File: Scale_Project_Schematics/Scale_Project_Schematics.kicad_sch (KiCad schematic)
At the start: 0 parts

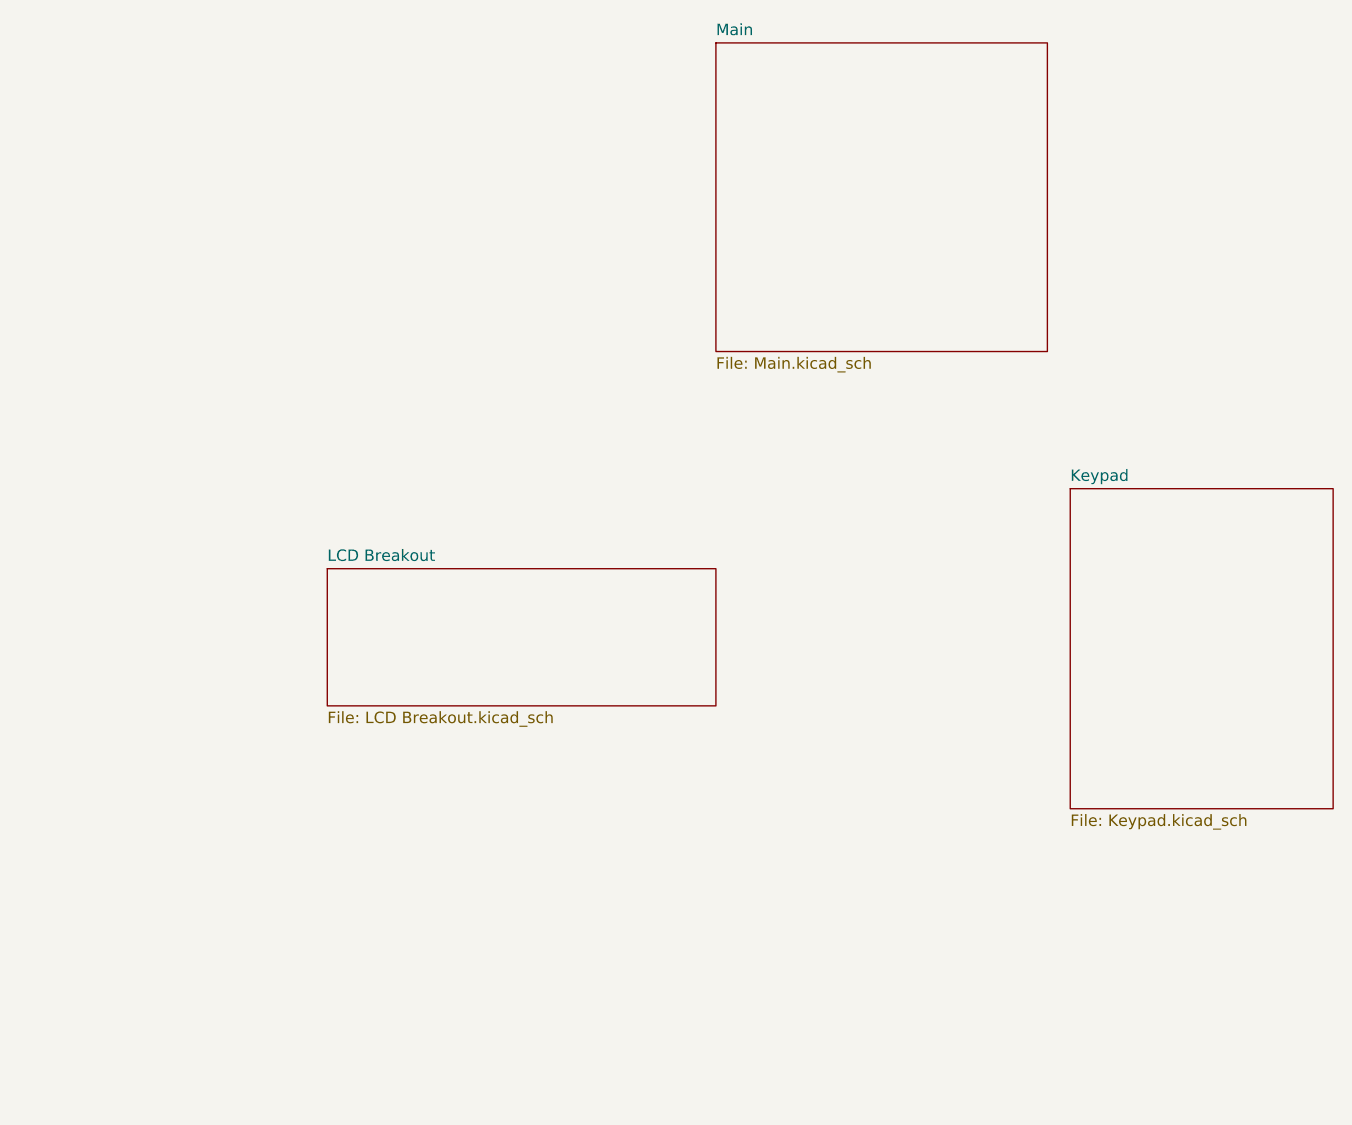
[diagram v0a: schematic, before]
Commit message: Adds Power sheet
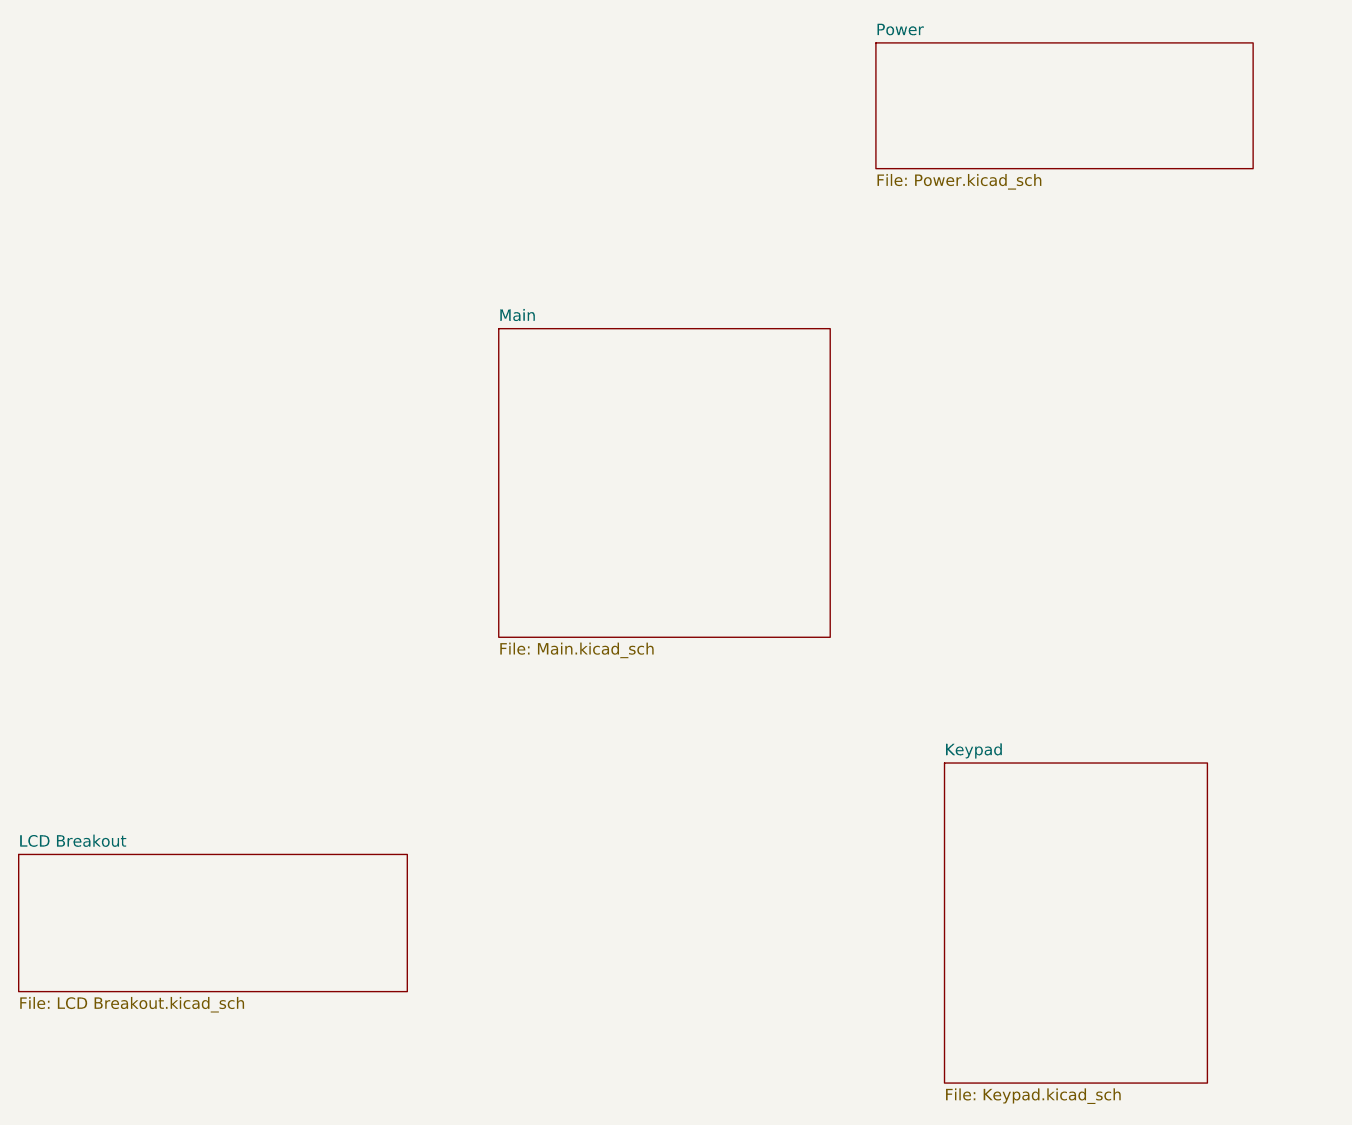
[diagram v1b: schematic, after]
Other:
- added sheet Power (Power.kicad_sch)
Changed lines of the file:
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@@
 	(paper "A4")
 	(sheet
-		(at 160.02 86.36)
+		(at 138.43 36.83)
+		(size 41.91 13.97)
+		(exclude_from_sim no)
+		(in_bom yes)
+		(on_board yes)
+		(dnp no)
+		(fields_autoplaced yes)
+		(stroke
+			(width 0.1524)
+			(type solid)
+		)
+		(fill
+			(color 0 0 0 0.0000)
+		)
+		(property "Sheetname" "Power"
+			(at 138.43 36.1184 0)
+			(effects
+				(font
+					(size 1.27 1.27)
+				)
+				(justify left bottom)
+			)
+		)
+		(property "Sheetfile" "Power.kicad_sch"
+			(at 138.43 51.3846 0)
+			(effects
+				(font
+					(size 1.27 1.27)
+				)
+				(justify left top)
+			)
+		)
+		(instances
+			(project "Scale_Project_Schematics"
+				(path "/3cf07eb0-0061-4372-8fed-c89eb2646bb2"
+					(page "5")
+				)
+			)
+		)
+	)
+	(sheet
+		(at 146.05 116.84)
 		(size 29.21 35.56)
 		(exclude_from_sim no)
@@
 		)
 		(property "Sheetname" "Keypad"
-			(at 160.02 85.6484 0)
+			(at 146.05 116.1284 0)
 			(effects
 				(font
@@
 		)
 		(property "Sheetfile" "Keypad.kicad_sch"
-			(at 160.02 122.5046 0)
+			(at 146.05 152.9846 0)
 			(effects
 				(font
@@
 	)
 	(sheet
-		(at 77.47 95.25)
+		(at 43.18 127)
 		(size 43.18 15.24)
 		(exclude_from_sim no)
@@
 		)
 		(property "Sheetname" "LCD Breakout"
-			(at 77.47 94.5384 0)
+			(at 43.18 126.2884 0)
 			(effects
 				(font
@@
 		)
 		(property "Sheetfile" "LCD Breakout.kicad_sch"
-			(at 77.47 111.0746 0)
+			(at 43.18 142.8246 0)
 			(effects
 				(font
@@
 	)
 	(sheet
-		(at 120.65 36.83)
+		(at 96.52 68.58)
 		(size 36.83 34.29)
 		(exclude_from_sim no)
@@
 		)
 		(property "Sheetname" "Main"
-			(at 120.65 36.1184 0)
+			(at 96.52 67.8684 0)
 			(effects
 				(font
@@
 		)
 		(property "Sheetfile" "Main.kicad_sch"
-			(at 120.65 71.7046 0)
+			(at 96.52 103.4546 0)
 			(effects
 				(font
@@
 		)
 		(property "Field2" ""
-			(at 120.65 36.83 0)
+			(at 96.52 68.58 0)
 			(effects
 				(font
